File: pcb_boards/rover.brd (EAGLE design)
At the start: 2.5 x 2.5 mm, 16 parts, among them IC1 MC33269ST-5.0T3, J1 B02B-PASK(LF)(SN)

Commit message: finished pcb, added BOM
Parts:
- removed J1: B02B-PASK(LF)(SN), Headers:B02B-PASK(LF)(SN)
- added ESC, PWR_IN, SERVO: JST-XH-02-PIN-LONG-PAD, Rembrandt Electronics - JST XH Connectors v1-0:JST-XH-02-PACKAGE-LONG-PAD
- added RECIEVER: JST-XH-03-PIN-LONG-PAD, Rembrandt Electronics - JST XH Connectors v1-0:JST-XH-03-PACKAGE-LONG-PAD
- added U$4, U$6, U$7, U$8: (no value), holes:3,6
- FL_ENC, FR_ENC, RL_ENC, RR_ENC: value B4B-XH-A(LF)(SN) -> JST-XH-04-PIN-LONG-PAD; device Headers:B4B-XH-A(LF)(SN) -> Rembrandt Electronics - JST XH Connectors v1-0:JST-XH-04-PACKAGE-LONG-PAD
- STEER_ENC: value B3B-ZR(LF)(SN) -> JST-XH-03-PIN-LONG-PAD; device Headers:B3B-ZR(LF)(SN) -> Rembrandt Electronics - JST XH Connectors v1-0:JST-XH-03-PACKAGE-LONG-PAD
- moved GREEN 27.1 mm to (43.2, 16.5)
- moved FR_ENC 26.7 mm to (17.8, 0.00), turned to 270 degrees
- moved STEER_ENC 25.3 mm to (17.8, 29.2), turned to 270 degrees
- moved R1 24.3 mm to (43.2, 20.3)
- moved FL_ENC 21.1 mm to (26.7, 0.00), turned to 270 degrees
- moved JP3 18.5 mm to (62.9, 34.3)
- moved JP4 18.5 mm to (62.9, 52.1)
- moved RR_ENC 18.3 mm to (17.8, 15.2), turned to 270 degrees
- moved U$5 18.2 mm to (58.4, 2.54)
- moved C2 15.5 mm to (36.8, 16.5)
- moved S1 14.9 mm to (38.1, 27.9)
- moved C1 12.0 mm to (36.8, 20.3)
- moved D1 10.2 mm to (44.5, 38.1), turned to 270 degrees
- moved IC1 8.52 mm to (38.1, 38.1)
- moved RL_ENC 4.02 mm to (26.7, 15.2), turned to 270 degrees
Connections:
- net ESC: now also ESC.1
- net GND: now also ESC.2, PWR_IN.2, RECIEVER.3, SERVO.2; no longer J1.2
- net PWRIN: now also PWR_IN.1; no longer J1.1
- net REC_ESC: now also RECIEVER.1
- net REC_SERVO: now also RECIEVER.2
- net SERVO: now also SERVO.1
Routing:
- net +5V: track 0.00 -> 158.7 mm
- net STEER_ENC: track 0.00 -> 66.3 mm, vias 0 -> 2
- net SERVO: track 0.00 -> 62.7 mm, vias 0 -> 1
- net ESC: track 0.00 -> 51.5 mm, vias 0 -> 1
- net REC_ESC: track 0.00 -> 47.0 mm, vias 0 -> 1
- net FR_ENC_A: track 0.00 -> 43.5 mm
- net REC_SERVO: track 0.00 -> 43.4 mm, vias 0 -> 1
- net SDA_5V: track 0.00 -> 43.4 mm
- net SCL_5V: track 0.00 -> 43.4 mm
- net FR_ENC_B: track 0.00 -> 40.1 mm
- net FL_ENC_A: track 0.00 -> 38.4 mm
- net FL_ENC_B: track 0.00 -> 36.6 mm
- net RR_ENC_A: track 0.00 -> 30.4 mm
- net PWRIN: track 0.00 -> 26.1 mm, vias 0 -> 1
- net N$2: track 0.00 -> 25.7 mm
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- added copper zone on layer 1, net GND
- added copper zone on layer 16, net GND
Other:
- board size 2.5 x 2.5 mm -> 61 x 59.7 mm

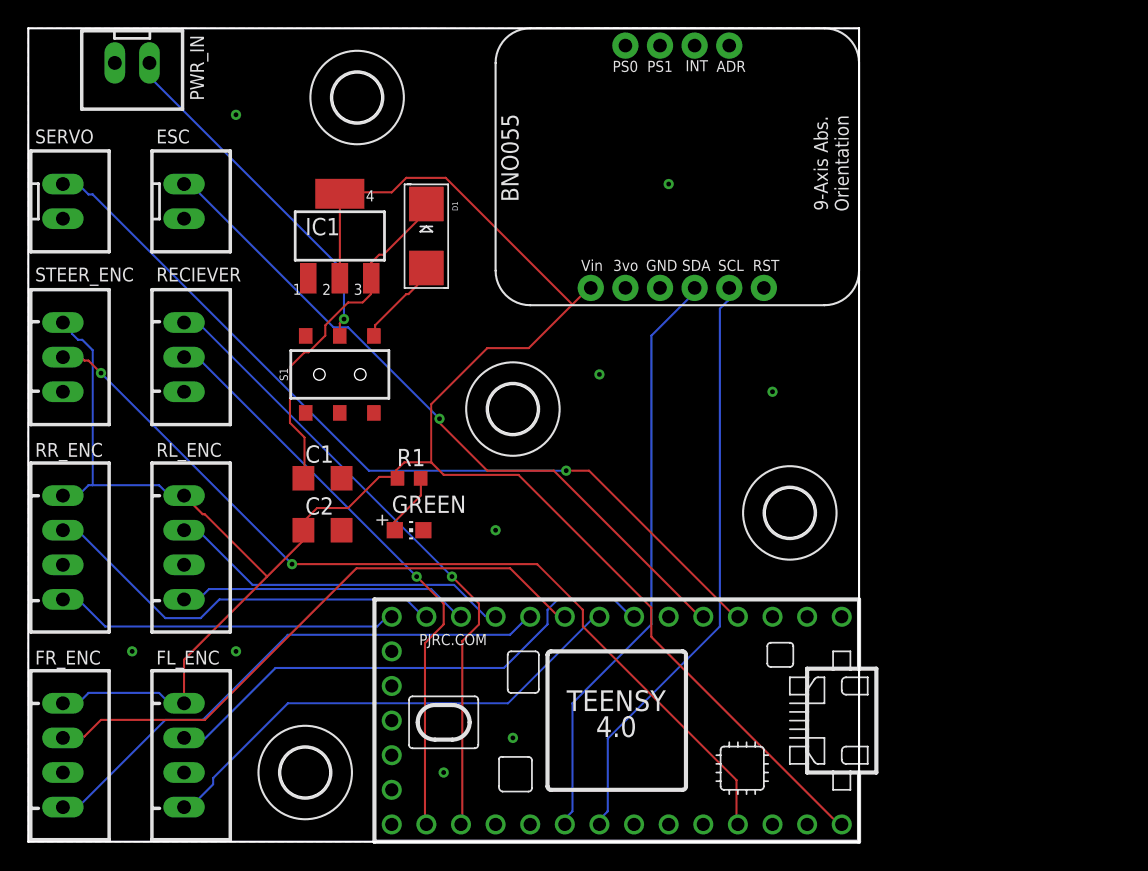
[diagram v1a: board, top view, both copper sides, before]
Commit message: changed LDO regulator to active one in stock
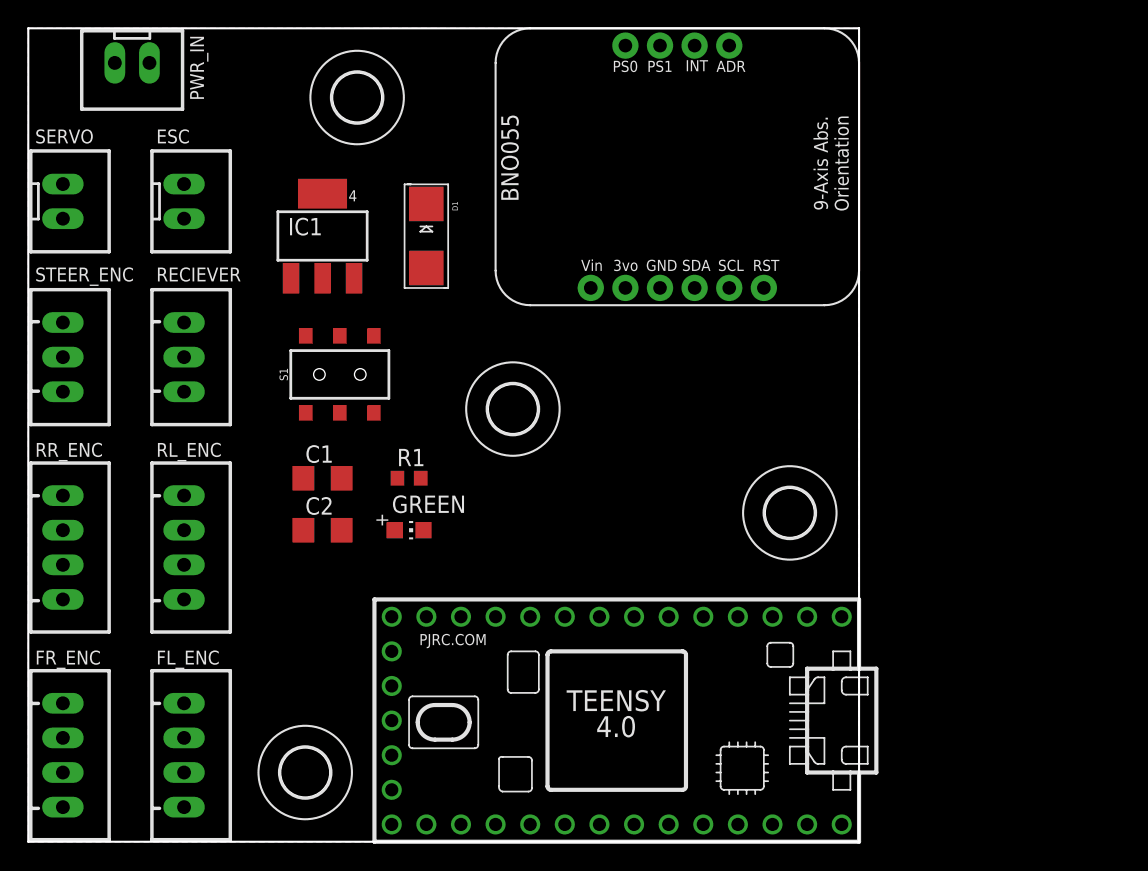
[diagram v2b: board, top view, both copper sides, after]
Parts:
- C1: value 47u -> 0.1u
- C2: value 47u -> 10u
- IC1: value MC33269ST-5.0T3 -> LM2937IMP-5.0; device linear:SOT223 -> lm2937:SOT223
- moved IC1 1.27 mm to (36.8, 38.1)
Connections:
- new net N$9: C2.2, IC1.GND
- net +5V: now also IC1.OUT; no longer C2.1, IC1.2, IC1.4
- net GND: now also C2.1, IC1.GND@; no longer C2.2, IC1.1
- net N$2: now also IC1.IN; no longer IC1.3
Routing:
- net +5V: track 158.7 -> 0.00 mm
- net STEER_ENC: track 66.3 -> 0.00 mm, vias 2 -> 0
- net SERVO: track 62.7 -> 0.00 mm, vias 1 -> 0
- net ESC: track 51.5 -> 0.00 mm, vias 1 -> 0
- net REC_ESC: track 47.0 -> 0.00 mm, vias 1 -> 0
- net FR_ENC_A: track 43.5 -> 0.00 mm
- net REC_SERVO: track 43.4 -> 0.00 mm, vias 1 -> 0
- net SDA_5V: track 43.4 -> 0.00 mm
- net SCL_5V: track 43.4 -> 0.00 mm
- net FR_ENC_B: track 40.1 -> 0.00 mm
- net FL_ENC_A: track 38.4 -> 0.00 mm
- net FL_ENC_B: track 36.6 -> 0.00 mm
- net RR_ENC_A: track 30.4 -> 0.00 mm
- net PWRIN: track 26.1 -> 0.00 mm, vias 1 -> 0
- net N$2: track 25.7 -> 0.00 mm
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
